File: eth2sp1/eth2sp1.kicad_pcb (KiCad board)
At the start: 2 copper layers, 60 x 18 mm, 2 parts, among them J1 GC_SP1, U1 ENC28J60_module

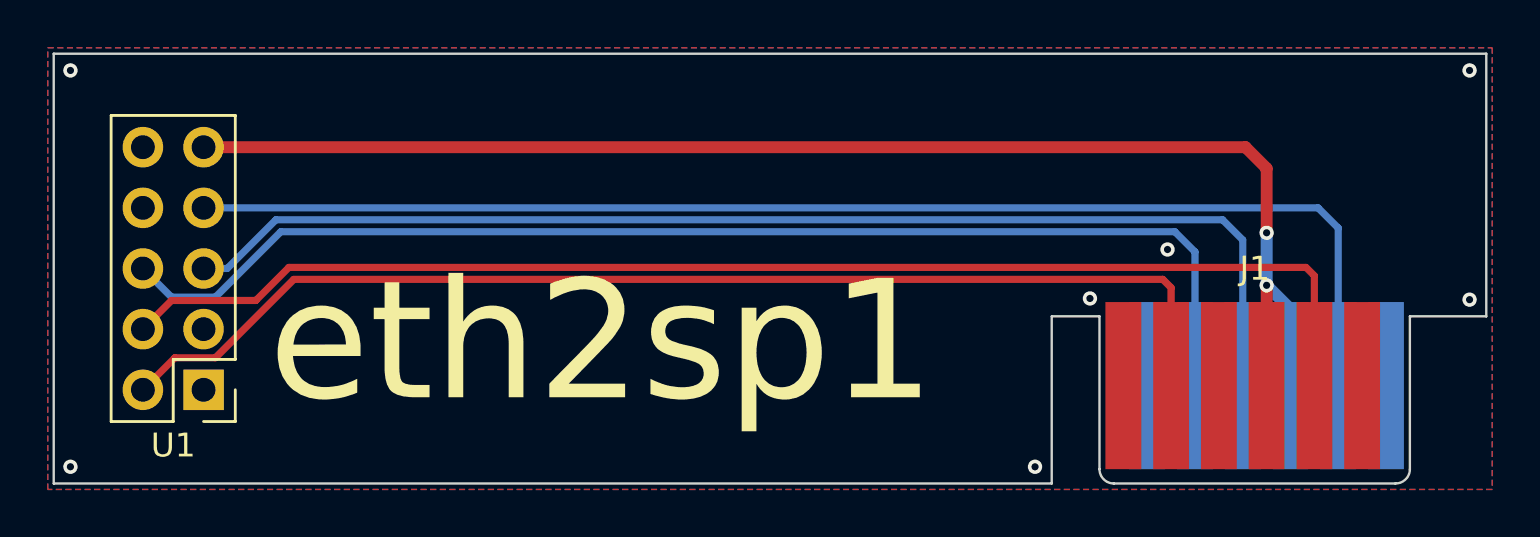
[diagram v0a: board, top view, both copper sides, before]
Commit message: Reversed SP1
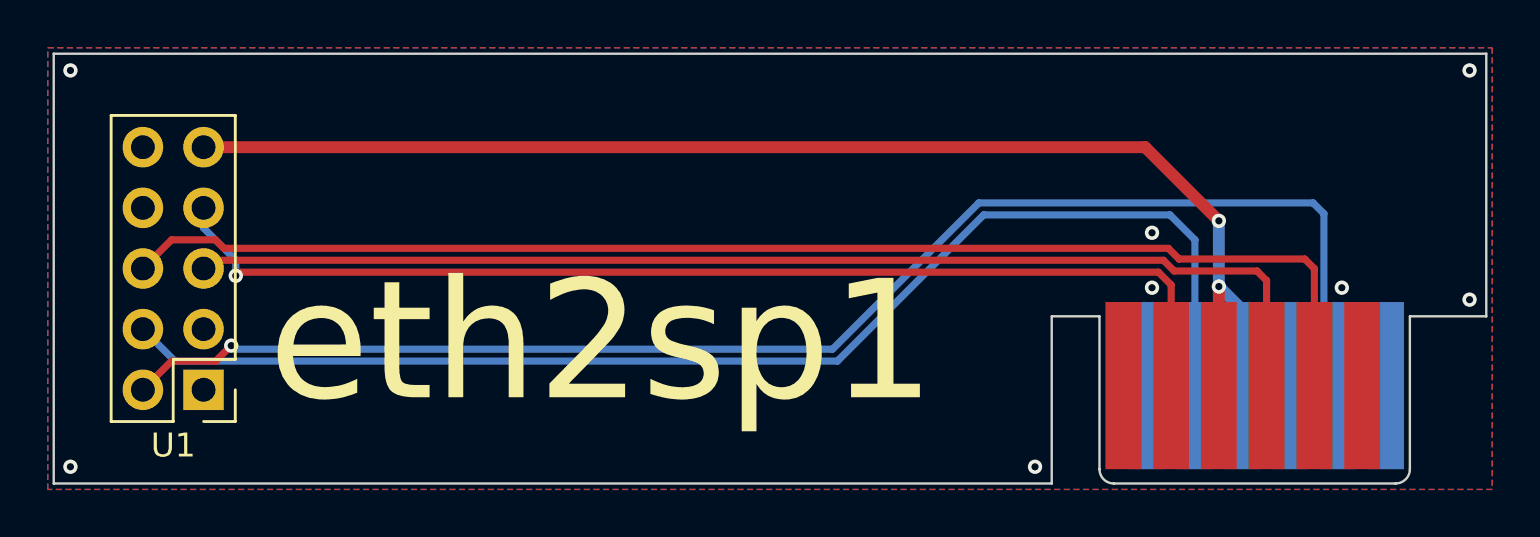
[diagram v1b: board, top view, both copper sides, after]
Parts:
- J1: moved to B.Cu
- turned J1 to 180 degrees
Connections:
- J1 pad 5: unconnected-(J1-12V-Pad5) -> (no net)
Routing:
- net /INT: track 49.2 -> 60.5 mm, vias 0 -> 1
- net /MOSI: track 54.5 -> 47.1 mm, vias 0 -> 1
- net +3V3: track 58.6 -> 55.3 mm
- net /SCK: track 51.6 -> 55.0 mm
- net /CS: track 50.8 -> 49.4 mm
- net /MISO: track 54.9 -> 53.7 mm
- net GND: vias 7 -> 8
